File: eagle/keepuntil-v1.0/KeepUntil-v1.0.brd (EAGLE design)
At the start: 26 x 36 mm, 17 parts, among them IC2 REG1117, Q1 CSTCR6M00G53Z, T1 BC846, U1 ATMEGA328P-AU, X1 MINI-USB-32005-201

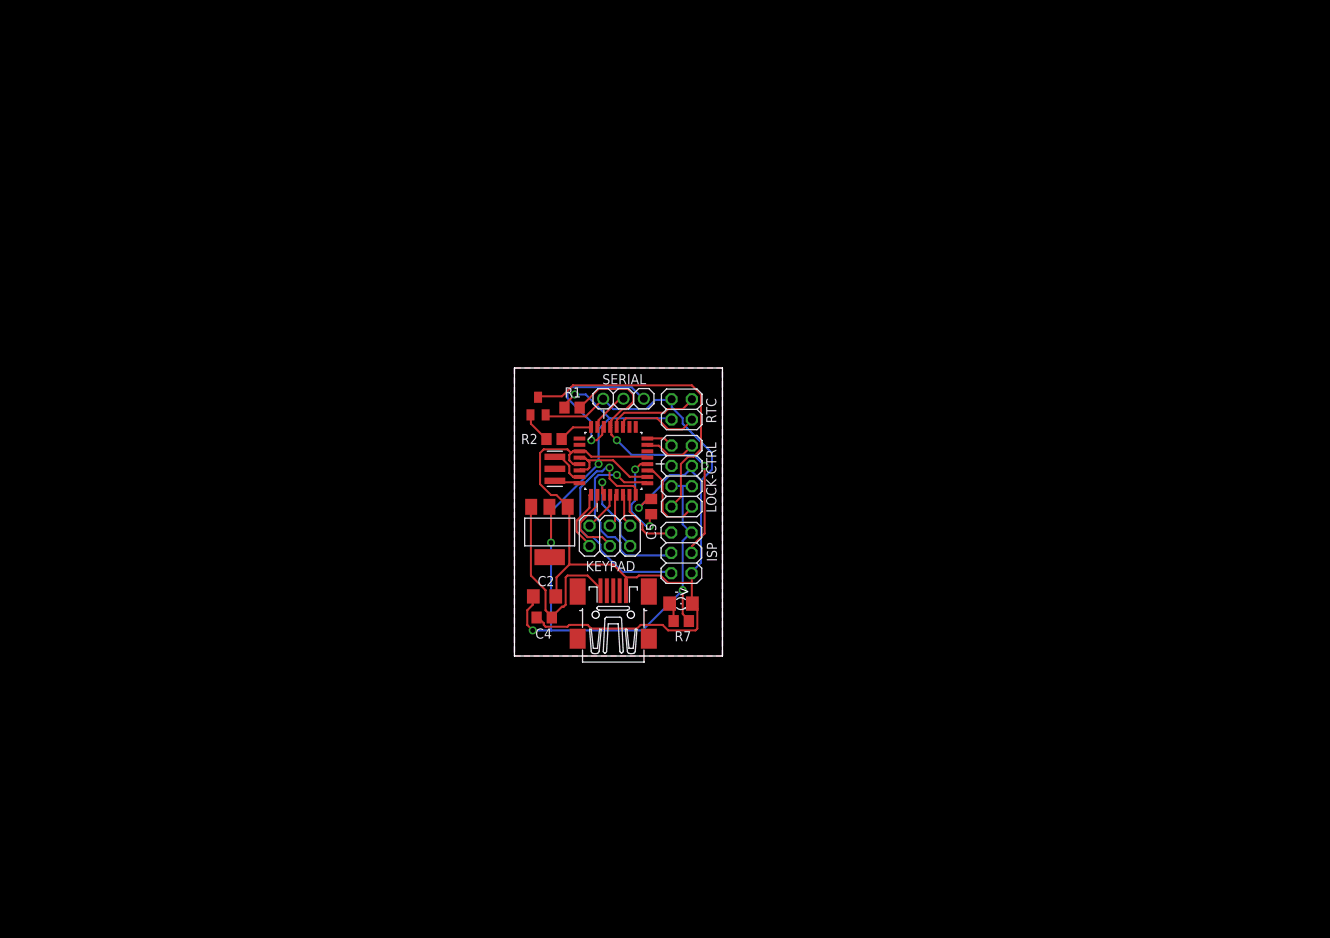
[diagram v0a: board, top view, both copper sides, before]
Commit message: pin header updates in schematic
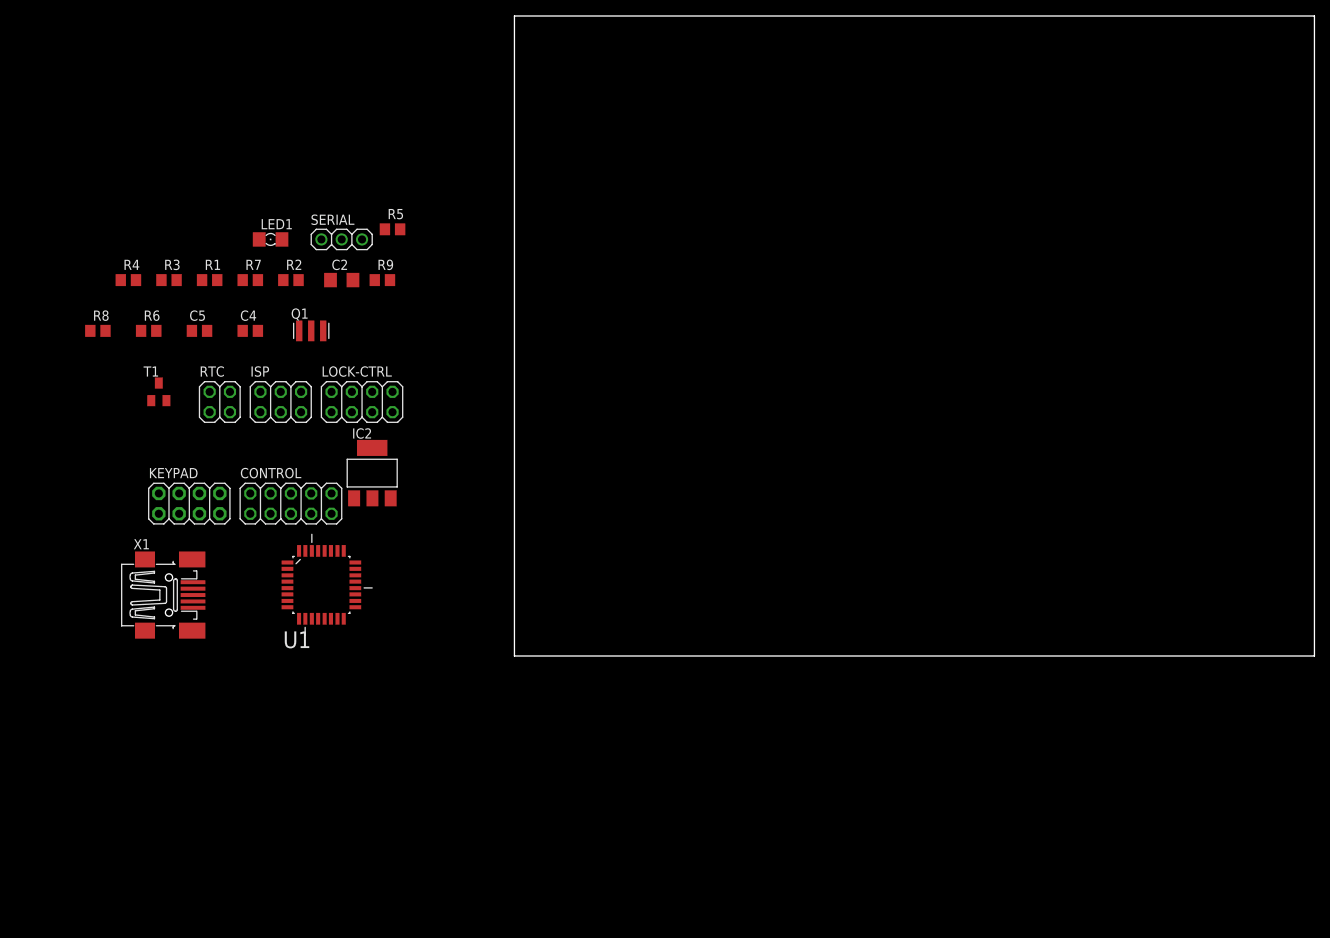
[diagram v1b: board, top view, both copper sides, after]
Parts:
- added CONTROL: (no value), pinhead:2X05
- added R3, R4, R5: 1K, resistor:R0805
- added R6, R8, R9: 4.7K, resistor:R0805
- KEYPAD: device pinhead:2X03 -> adafruit:2X04
- moved R7 68.7 mm to (-33.0, 47.0)
- moved LED1 68.6 mm to (-30.5, 52.1)
- moved C5 60.6 mm to (-39.4, 40.6), turned to 0 degrees
- moved RTC 57.7 mm to (-36.8, 31.8), turned to 0 degrees
- moved X1 55.6 mm to (-43.2, 7.62), turned to 0 degrees
- moved ISP 53.5 mm to (-29.2, 31.8), turned to 0 degrees
- moved KEYPAD 52.7 mm to (-40.6, 19.1)
- moved C4 51.3 mm to (-33.0, 40.6), turned to 0 degrees
- moved R1 48.0 mm to (-38.1, 47.0), turned to 0 degrees
- moved T1 47.4 mm to (-44.5, 33.0)
- moved C2 47.0 mm to (-21.6, 47.0)
- moved LOCK-CTRL 41.0 mm to (-19.1, 31.8), turned to 0 degrees
- moved SERIAL 40.5 mm to (-21.6, 52.1), turned to 0 degrees
- moved U1 39.7 mm to (-24.1, 8.89)
- moved R2 38.4 mm to (-27.9, 47.0)
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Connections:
- removed net COL1: KEYPAD.2, U1.12
- removed net COL2: KEYPAD.4, U1.13
- removed net COL3: KEYPAD.6, U1.14
- removed net ROW1: KEYPAD.1, U1.9
- removed net ROW2: KEYPAD.3, U1.10
- removed net ROW3: KEYPAD.5, U1.11
- new net N$10: U1.11
- new net N$11: U1.12
- new net N$12: U1.13
- new net N$13: U1.14
- new net N$14: U1.26
- new net N$6: U1.9
- new net N$9: U1.10
- net LED-GRN: no longer U1.23
- net LED-RED: no longer U1.24
- net SERVO: no longer U1.19
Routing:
- net GND: track 140.3 -> 0.00 mm, vias 1 -> 0
- net VCC: track 108.5 -> 0.00 mm, vias 5 -> 0
- net RESET: track 39.4 -> 0.00 mm, vias 2 -> 0
- net SOLENOID: track 37.4 -> 0.00 mm
- net MISO: track 29.9 -> 0.00 mm, vias 1 -> 0
- net N$4: track 26.2 -> 0.00 mm
- net SCK: track 24.7 -> 0.00 mm, vias 1 -> 0
- net RX: track 20.5 -> 0.00 mm, vias 1 -> 0
- net N$8: track 11.9 -> 0.00 mm, vias 2 -> 0
- net RTC-SCL: track 11.4 -> 0.00 mm
- net ROW3: track 11.1 -> 0.00 mm, vias 1 -> 0
- net SERVO: track 10.9 -> 0.00 mm
- net RTC-SDA: track 10.6 -> 0.00 mm
- net ROW2: track 9.89 -> 0.00 mm
- net MOSI: track 8.87 -> 0.00 mm
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- removed copper zone on layer 1, net GND
- removed copper zone on layer 16, net GND
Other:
- board size 26 x 36 mm -> 100 x 80 mm
- board text removed: "->"

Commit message: schematic
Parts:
- R1: value 1K -> 10K
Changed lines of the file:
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@@
 <attribute name="OC_NEWARK" value="25M8759" x="-25.4" y="40.64" size="1.778" layer="27" display="off"/>
 </element>
-<element name="R1" library="resistor" package="R0805" value="1K" x="-38.1" y="46.99"/>
+<element name="R1" library="resistor" package="R0805" value="10K" x="-38.1" y="46.99"/>
 <element name="R2" library="resistor" package="R0805" value="10K" x="-27.94" y="46.99"/>
 <element name="R3" library="resistor" package="R0805" value="1K" x="-43.18" y="46.99"/>

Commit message: schematic
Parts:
- added S1: SWITCH-MOMENTARY-2SMD-1101NE, SparkFun-Electromechanical:TACTILE-SWITCH-1101NE
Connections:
- net GND: now also S1.1
- net RESET: now also S1.2
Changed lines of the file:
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@@
 <attribute name="OC_NEWARK" value="unknown" x="-43.18" y="7.62" size="1.778" layer="27" display="off"/>
+</element>
+<element name="S1" library="SparkFun-Electromechanical" package="TACTILE-SWITCH-1101NE" value="SWITCH-MOMENTARY-2SMD-1101NE" x="-49.53" y="-3.81">
+<attribute name="PROD_ID" value="SWCH-00815" x="-49.53" y="-3.81" size="1.778" layer="27" display="off"/>
 </element>
 </elements>
@@
 <contactref element="R1" pad="1"/>
 <contactref element="ISP" pad="4"/>
+<contactref element="S1" pad="2"/>
+<wire x1="-24.5364" y1="13.1318" x2="-46.38" y2="-3.81" width="0" layer="19" extent="1-1"/>
 <wire x1="-29.21" y1="33.02" x2="-24.5364" y2="13.1318" width="0" layer="19" extent="1-1"/>
 <wire x1="-39.05" y1="46.99" x2="-29.21" y2="33.02" width="0" layer="19" extent="1-1"/>
@@
 <contactref element="LOCK-CTRL" pad="5"/>
 <contactref element="SERIAL" pad="3"/>
+<contactref element="S1" pad="1"/>
+<wire x1="-40.18" y1="6.02" x2="-52.68" y2="-3.81" width="0" layer="19" extent="1-1"/>
 <wire x1="-28.3718" y1="8.4836" x2="-40.18" y2="6.02" width="0" layer="19" extent="1-1"/>
 <wire x1="-28.3718" y1="10.0838" x2="-28.3718" y2="8.4836" width="0" layer="19" extent="1-1"/>

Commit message: schematic
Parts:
- removed CONTROL: (no value), pinhead:2X05
- removed KEYPAD: (no value), adafruit:2X04
- removed LOCK-CTRL: (no value), pinhead:2X04
- removed RTC: (no value), pinhead:2X02
- removed SERIAL: (no value), adafruit:1X03
- added JP1: (no value), pinhead:2X06
- added JP2: (no value), pinhead:2X04
- moved R8 79.6 mm to (26.7, 29.2), turned to 270 degrees
- moved R9 45.4 mm to (26.7, 33.0), turned to 270 degrees
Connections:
- removed net LED-GRN: LOCK-CTRL.7
- removed net LED-RED: LOCK-CTRL.8
- removed net SERVO: LOCK-CTRL.1
- new net COL1: JP2.1
- new net COL2: JP2.3
- new net COL3: JP2.5
- new net N$15: R3.2
- new net N$16: R4.1
- new net N$17: R4.2
- new net N$18: R5.1
- new net N$19: R6.1
- new net N$22: R5.2
- new net N$23: R6.2
- new net N$5: R3.1
- new net ROW1: JP2.2, R9.1
- new net ROW2: JP2.4, R8.1, R9.2
- new net ROW3: JP2.6, R8.2
- net GND: no longer LOCK-CTRL.5, RTC.4, SERIAL.3
- net RTC-SCL: no longer RTC.3
- net RTC-SDA: no longer RTC.1
- net RX: no longer SERIAL.1
- net SOLENOID: no longer LOCK-CTRL.2
- net TX: no longer SERIAL.2
- net VCC: no longer LOCK-CTRL.3, LOCK-CTRL.4, RTC.2
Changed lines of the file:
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@@
 <element name="C4" library="resistor" package="C0805" value="0.1uF" x="-33.02" y="40.64"/>
 <element name="C5" library="resistor" package="C0805" value="0.1uF" x="-39.37" y="40.64"/>
-<element name="CONTROL" library="pinhead" package="2X05" value="" x="-27.94" y="19.05"/>
 <element name="IC2" library="burr-brown" package="SOT223" value="REG1117" x="-17.78" y="22.86">
 <attribute name="OC_FARNELL" value="1097566" x="-17.78" y="22.86" size="1.778" layer="27" display="off"/>
@@
 </element>
 <element name="ISP" library="pinhead" package="2X03" value="" x="-29.21" y="31.75"/>
-<element name="KEYPAD" library="adafruit" package="2X04" value="" x="-40.64" y="19.05"/>
 <element name="LED1" library="led" package="1206" value="" x="-30.48" y="52.07"/>
-<element name="LOCK-CTRL" library="pinhead" package="2X04" value="" x="-19.05" y="31.75"/>
 <element name="Q1" library="murata-filter" package="CSTCR6M" value="CSTCR6M00G53Z" x="-25.4" y="40.64">
 <attribute name="OC_FARNELL" value="1170434" x="-25.4" y="40.64" size="1.778" layer="27" display="off"/>
@@
 <element name="R6" library="resistor" package="R0805" value="4.7K" x="-45.72" y="40.64"/>
 <element name="R7" library="resistor" package="R0805" value="330" x="-33.02" y="46.99"/>
-<element name="R8" library="resistor" package="R0805" value="4.7K" x="-52.07" y="40.64"/>
-<element name="R9" library="resistor" package="R0805" value="4.7K" x="-16.51" y="46.99"/>
-<element name="RTC" library="pinhead" package="2X02" value="" x="-36.83" y="31.75"/>
-<element name="SERIAL" library="adafruit" package="1X03" value="" x="-21.59" y="52.07"/>
+<element name="R8" library="resistor" package="R0805" value="4.7K" x="26.67" y="29.21" rot="R270"/>
+<element name="R9" library="resistor" package="R0805" value="4.7K" x="26.67" y="33.02" rot="R270"/>
 <element name="T1" library="transistor" package="SOT23" value="BC846" x="-44.45" y="33.02"/>
 <element name="U1" library="Ava" package="QFP80P900X900X120-32N" value="ATMEGA328P-AU" x="-24.13" y="8.89">
@@
 <attribute name="PROD_ID" value="SWCH-00815" x="-49.53" y="-3.81" size="1.778" layer="27" display="off"/>
 </element>
+<element name="JP1" library="pinhead" package="2X06" value="" x="-54.61" y="-12.7"/>
+<element name="JP2" library="pinhead" package="2X04" value="" x="22.86" y="30.48" rot="R270"/>
 </elements>
 <signals>
@@
 <signal name="RTC-SCL">
 <contactref element="U1" pad="28"/>
-<contactref element="RTC" pad="3"/>
-<wire x1="-35.56" y1="30.48" x2="-23.7236" y2="13.1318" width="0" layer="19" extent="1-1"/>
 </signal>
 <signal name="TX">
 <contactref element="U1" pad="31"/>
-<contactref element="SERIAL" pad="2"/>
-<wire x1="-26.1366" y1="13.1318" x2="-21.59" y2="52.07" width="0" layer="19" extent="1-1"/>
 </signal>
 <signal name="RX">
 <contactref element="U1" pad="30"/>
-<contactref element="SERIAL" pad="1"/>
-<wire x1="-25.3238" y1="13.1318" x2="-24.13" y2="52.07" width="0" layer="19" extent="1-1"/>
-</signal>
-<signal name="SERVO">
-<contactref element="LOCK-CTRL" pad="1"/>
 </signal>
 <signal name="SOLENOID-SIG">
@@
 <wire x1="-26.924" y1="13.1318" x2="-26.99" y2="46.99" width="0" layer="19" extent="1-1"/>
 </signal>
-<signal name="LED-GRN">
-<contactref element="LOCK-CTRL" pad="7"/>
-</signal>
-<signal name="LED-RED">
-<contactref element="LOCK-CTRL" pad="8"/>
-</signal>
 <signal name="N$3">
 <contactref element="R2" pad="1"/>
@@
 </signal>
 <signal name="SOLENOID">
-<contactref element="LOCK-CTRL" pad="2"/>
 <contactref element="T1" pad="3"/>
-<wire x1="-44.45" y1="34.12" x2="-22.86" y2="33.02" width="0" layer="19" extent="1-1"/>
 </signal>
 <signal name="RTC-SDA">
 <contactref element="U1" pad="27"/>
-<contactref element="RTC" pad="1"/>
-<wire x1="-38.1" y1="30.48" x2="-22.9362" y2="13.1318" width="0" layer="19" extent="1-1"/>
 </signal>
 <signal name="VCC">
@@
 <contactref element="U1" pad="4"/>
 <contactref element="ISP" pad="2"/>
-<contactref element="RTC" pad="2"/>
-<contactref element="LOCK-CTRL" pad="3"/>
-<contactref element="LOCK-CTRL" pad="4"/>
 <contactref element="IC2" pad="2"/>
 <contactref element="C2" pad="1"/>
@@
 <wire x1="-37.15" y1="46.99" x2="-32.07" y2="46.99" width="0" layer="19" extent="1-1"/>
 <wire x1="-31.75" y1="33.02" x2="-32.07" y2="46.99" width="0" layer="19" extent="1-1"/>
-<wire x1="-38.1" y1="33.02" x2="-31.75" y2="33.02" width="0" layer="19" extent="1-1"/>
-<wire x1="-20.32" y1="33.02" x2="-31.75" y2="33.02" width="0" layer="19" extent="1-1"/>
-<wire x1="-20.32" y1="30.48" x2="-20.32" y2="33.02" width="0" layer="19" extent="1-1"/>
-<wire x1="-17.7546" y1="19.7104" x2="-20.32" y2="30.48" width="0" layer="19" extent="1-1"/>
+<wire x1="-17.7546" y1="19.7104" x2="-31.75" y2="33.02" width="0" layer="19" extent="1-1"/>
 <wire x1="-19.8882" y1="6.8834" x2="-17.7546" y2="19.7104" width="0" layer="19" extent="1-1"/>
 <wire x1="-28.3718" y1="7.6962" x2="-19.8882" y2="6.8834" width="0" layer="19" extent="1-1"/>
@@
 <contactref element="T1" pad="2"/>
 <contactref element="ISP" pad="6"/>
-<contactref element="RTC" pad="4"/>
 <contactref element="X1" pad="5"/>
-<contactref element="LOCK-CTRL" pad="5"/>
-<contactref element="SERIAL" pad="3"/>
 <contactref element="S1" pad="1"/>
 <wire x1="-40.18" y1="6.02" x2="-52.68" y2="-3.81" width="0" layer="19" extent="1-1"/>
@@
 <wire x1="-19.8882" y1="9.2964" x2="-28.3718" y2="8.4836" width="0" layer="19" extent="1-1"/>
 <wire x1="-20.0406" y1="19.7104" x2="-19.8882" y2="9.2964" width="0" layer="19" extent="1-1"/>
-<wire x1="-17.78" y1="30.48" x2="-20.0406" y2="19.7104" width="0" layer="19" extent="1-1"/>
-<wire x1="-26.67" y1="33.02" x2="-17.78" y2="30.48" width="0" layer="19" extent="1-1"/>
-<wire x1="-35.56" y1="33.02" x2="-26.67" y2="33.02" width="0" layer="19" extent="1-1"/>
-<wire x1="-43.5" y1="31.92" x2="-35.56" y2="33.02" width="0" layer="19" extent="1-1"/>
-<wire x1="-38.42" y1="40.64" x2="-35.56" y2="33.02" width="0" layer="19" extent="1-1"/>
-<wire x1="-32.07" y1="40.64" x2="-38.42" y2="40.64" width="0" layer="19" extent="1-1"/>
+<wire x1="-26.67" y1="33.02" x2="-20.0406" y2="19.7104" width="0" layer="19" extent="1-1"/>
+<wire x1="-32.07" y1="40.64" x2="-26.67" y2="33.02" width="0" layer="19" extent="1-1"/>
+<wire x1="-38.42" y1="40.64" x2="-32.07" y2="40.64" width="0" layer="19" extent="1-1"/>
+<wire x1="-43.5" y1="31.92" x2="-38.42" y2="40.64" width="0" layer="19" extent="1-1"/>
 <wire x1="-29.058" y1="52.07" x2="-32.07" y2="40.64" width="0" layer="19" extent="1-1"/>
-<wire x1="-19.05" y1="52.07" x2="-29.058" y2="52.07" width="0" layer="19" extent="1-1"/>
-<wire x1="-20.19" y1="46.99" x2="-19.05" y2="52.07" width="0" layer="19" extent="1-1"/>
+<wire x1="-20.19" y1="46.99" x2="-29.058" y2="52.07" width="0" layer="19" extent="1-1"/>
 </signal>
 <signal name="N$4">
@@
 <contactref element="U1" pad="26"/>
 </signal>
+<signal name="ROW1">
+<contactref element="R9" pad="1"/>
+<contactref element="JP2" pad="2"/>
+<wire x1="24.13" y1="34.29" x2="26.67" y2="33.97" width="0" layer="19" extent="1-1"/>
+</signal>
+<signal name="ROW2">
+<contactref element="R9" pad="2"/>
+<contactref element="R8" pad="1"/>
+<contactref element="JP2" pad="4"/>
+<wire x1="26.67" y1="30.16" x2="24.13" y2="31.75" width="0" layer="19" extent="1-1"/>
+<wire x1="26.67" y1="32.07" x2="26.67" y2="30.16" width="0" layer="19" extent="1-1"/>
+</signal>
+<signal name="ROW3">
+<contactref element="R8" pad="2"/>
+<contactref element="JP2" pad="6"/>
+<wire x1="26.67" y1="28.26" x2="24.13" y2="29.21" width="0" layer="19" extent="1-1"/>
+</signal>
+<signal name="N$5">
+<contactref element="R3" pad="1"/>
+</signal>
+<signal name="N$15">
+<contactref element="R3" pad="2"/>
+</signal>
+<signal name="N$16">
+<contactref element="R4" pad="1"/>
+</signal>
+<signal name="N$17">
+<contactref element="R4" pad="2"/>
+</signal>
+<signal name="N$18">
+<contactref element="R5" pad="1"/>
+</signal>
+<signal name="N$19">
+<contactref element="R6" pad="1"/>
+</signal>
+<signal name="N$22">
+<contactref element="R5" pad="2"/>
+</signal>
+<signal name="N$23">
+<contactref element="R6" pad="2"/>
+</signal>
+<signal name="COL1">
+<contactref element="JP2" pad="1"/>
+</signal>
+<signal name="COL2">
+<contactref element="JP2" pad="3"/>
+</signal>
+<signal name="COL3">
+<contactref element="JP2" pad="5"/>
+</signal>
 </signals>
